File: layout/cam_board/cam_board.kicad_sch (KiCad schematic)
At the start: 76 parts, among them J2 USB Connector, J3 BATT_CONNECTOR, J4 LCD conn, J5 Stick conn, J6 Conn_01x05_Pin, SW1 BOOT0, SW2 NRST, SW3 USER, SW4 ON/OFF, U1 STM32F401CCUx, U2 USBLC6-2SC6, U3 M24C16-RMN6TP, U4 AP2112K-3.3, U5 MCP73871-1AA, Y1 ECS-80-18-23B-JTN-TR, Y2 SC32S-7PF20PPM

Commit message: Update board and layout
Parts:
- removed J6: Conn_01x05_Pin, Connector_PinHeader_1.27mm:PinHeader_1x05_P1.27mm_Vertical, symbol Connector:Conn_01x05_Pin
- added J1: Conn_01x06_Pin, Connector_PinHeader_1.27mm:PinHeader_1x06_P1.27mm_Vertical, symbol Connector:Conn_01x06_Pin
- added JP5, JP6: SolderJumper_2_Open, Jumper:SolderJumper-2_P1.3mm_Open_RoundedPad1.0x1.5mm, symbol Jumper:SolderJumper_2_Open
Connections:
- net +3V3: now also JP5.1 (A), JP6.2 (B); no longer C17.1, U4.5 (VOUT)
- net GND: now also J1.2 (Pin_2)
- net NRST: now also J1.6 (Pin_6)
- net SWCLK: now also J1.3 (Pin_3)
- net SWDIO: now also J1.4 (Pin_4)
- net SWO: now also J1.5 (Pin_5)
- new net: C17.1, JP6.1 (A), U4.5 (VOUT)
- new net: J1.1 (Pin_1), JP5.2 (B)

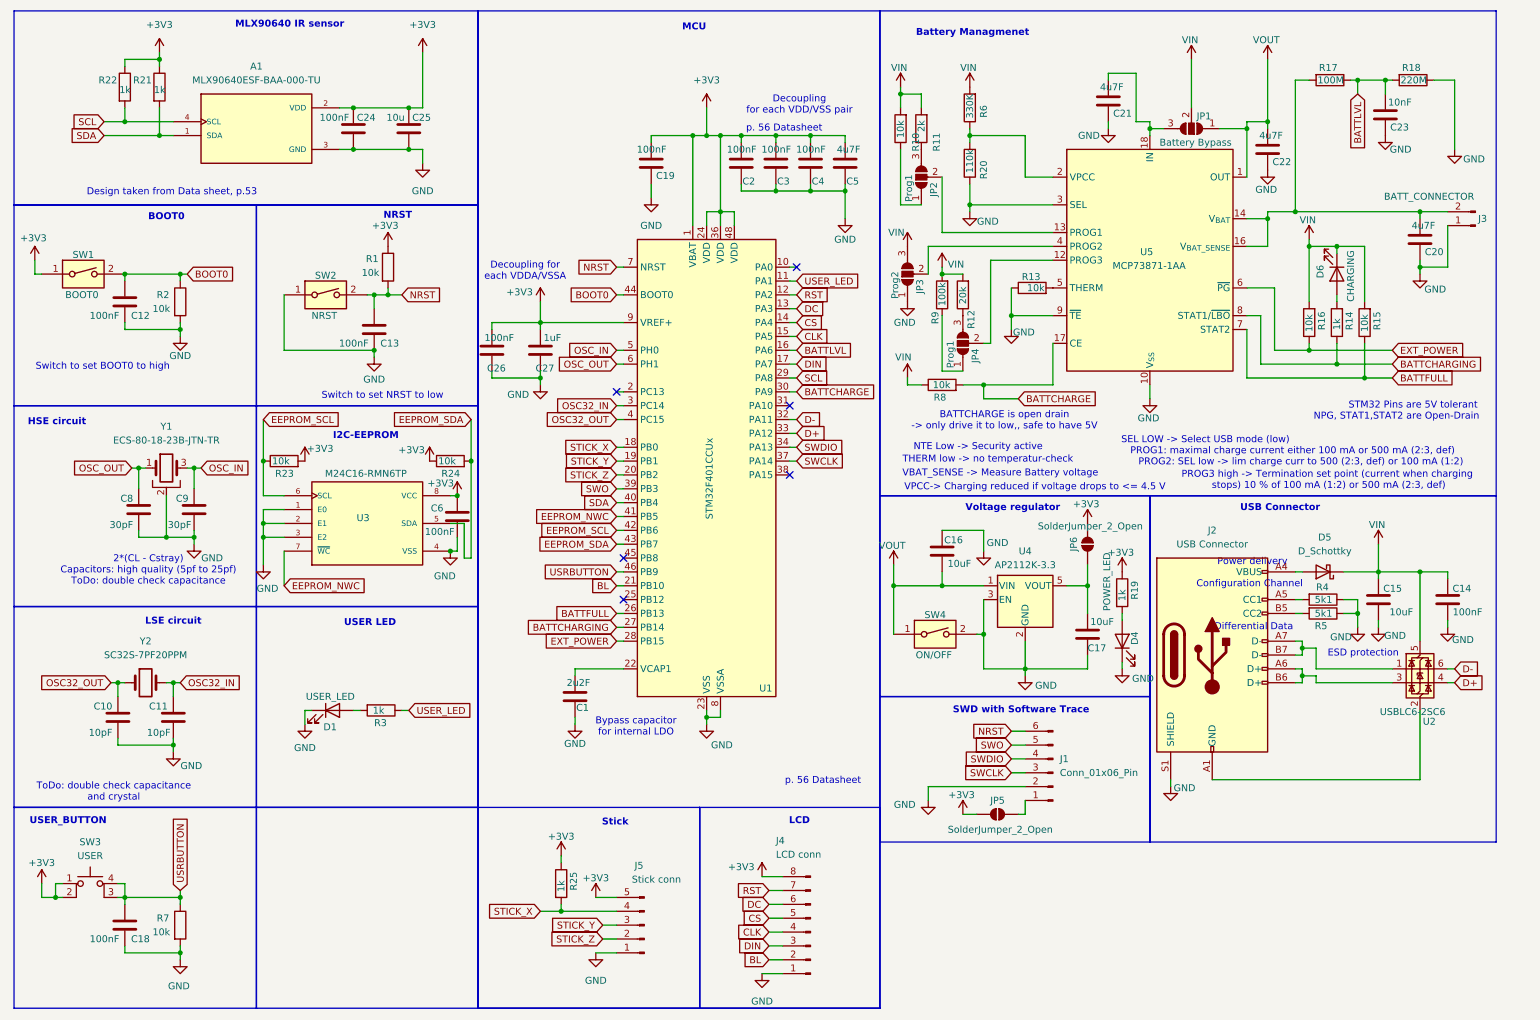
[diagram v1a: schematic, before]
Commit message: add to main loop, update layout and schematic
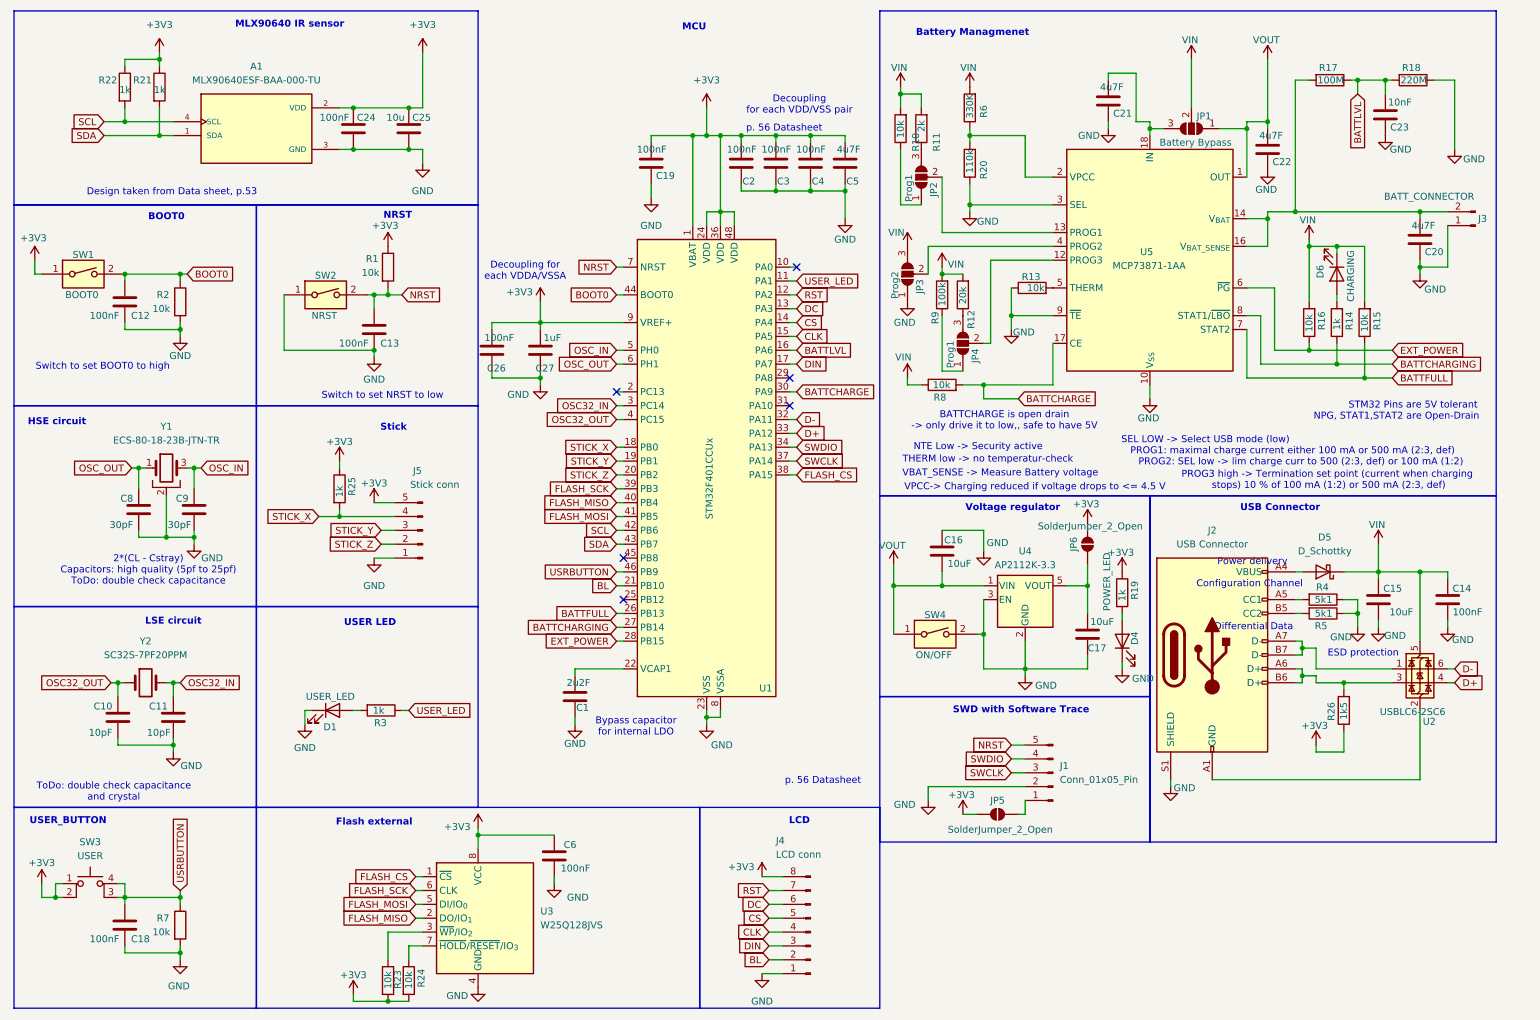
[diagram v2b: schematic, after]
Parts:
- removed J1: Conn_01x06_Pin, Connector_PinHeader_1.27mm:PinHeader_1x06_P1.27mm_Vertical, symbol Connector:Conn_01x06_Pin
- removed U3: M24C16-RMN6TP, A_Custom:SOIC127P600X175-8N, symbol Custom:M24C16-RMN6TP
- added J1: Conn_01x05_Pin, Connector_PinHeader_1.27mm:PinHeader_1x05_P1.27mm_Vertical, symbol Connector:Conn_01x05_Pin
- added R26: 1k5, Resistor_SMD:R_0603_1608Metric_Pad0.98x0.95mm_HandSolder, symbol Device:R
- added U3: W25Q128JVS, Package_SO:SOIC-8_5.3x5.3mm_P1.27mm, symbol Memory_Flash:W25Q128JVS
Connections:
- net +3V3: now also R24.2, R26.1, U3.8 (VCC); no longer R24.1
- net GND: now also J1.2 (Pin_2), U3.4 (GND)
- net NRST: now also J1.5 (Pin_5)
- net SCL: now also U1.42 (PB6); no longer U1.29 (PA8)
- net SDA: now also U1.43 (PB7); no longer U1.40 (PB4)
- net SWCLK: now also J1.3 (Pin_3)
- net SWDIO: now also J1.4 (Pin_4)
- net FLASH_CS: now reaches U1.38 (PA15)
- net FLASH_CS: now also U3.1 (~{CS})
- net at JP5.2 (B): now also J1.1 (Pin_1)
- net at J2.A6 (D+), J2.B6 (D+), U2.3 (I/O2): now also R26.2
- net EEPROM_NWC renamed FLASH_MOSI
- net FLASH_MOSI: now also U3.5 (DI/IO_{0})
- net EEPROM_SCL: no longer names the net of R23.1
- net EEPROM_SCL: now also U3.3 (~{WP}/IO_{2}); no longer U1.42 (PB6)
- removed net EEPROM_SDA: R24.2, U1.43 (PB7)
- net SWO renamed FLASH_SCK
- net FLASH_SCK: now also U3.6 (CLK)
- new net: R24.1, U3.7 (~{HOLD}/~{RESET}/IO_{3})
- new net FLASH_MISO: U1.40 (PB4), U3.2 (DO/IO_{1})
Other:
- note added: "Flash external"
- note removed: "I2C-EEPROM"
- moved on the sheet: J5, R25

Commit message: Update layout
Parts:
- added R27: 100k, Resistor_SMD:R_0603_1608Metric_Pad0.98x0.95mm_HandSolder, symbol Device:R
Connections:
- net GND: now also R27.1; no longer SW4.2, U4.3 (EN)
- new net: R27.2, SW4.2, U4.3 (EN)
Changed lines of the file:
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@@
 	)
 	(junction
+		(at 190.5 127)
+		(diameter 0)
+		(color 0 0 0 0)
+	)
+	(junction
 		(at 81.28 194.31)
 		(diameter 0)
@@
 	)
 	(junction
-		(at 190.5 127)
-		(diameter 0)
-		(color 0 0 0 0)
-	)
-	(junction
 		(at 238.76 34.29)
 		(diameter 0)
@@
 	)
 	(junction
-		(at 198.12 133.35)
+		(at 152.4 45.72)
 		(diameter 0)
 		(color 0 0 0 0)
 	)
 	(junction
-		(at 152.4 45.72)
+		(at 198.12 134.62)
 		(diameter 0)
 		(color 0 0 0 0)
@@
 	(wire
 		(pts
-			(xy 209.55 130.81) (xy 209.55 133.35)
+			(xy 209.55 130.81) (xy 209.55 134.62)
 		)
 		(stroke
@@
 	(wire
 		(pts
+			(xy 190.5 134.62) (xy 198.12 134.62)
+		)
+		(stroke
+			(width 0)
+			(type default)
+		)
+	)
+	(wire
+		(pts
 			(xy 139.7 142.24) (xy 139.7 143.51)
 		)
@@
 	(wire
 		(pts
-			(xy 209.55 133.35) (xy 198.12 133.35)
+			(xy 209.55 134.62) (xy 198.12 134.62)
 		)
 		(stroke
@@
 	(wire
 		(pts
-			(xy 198.12 134.62) (xy 198.12 133.35)
+			(xy 198.12 128.27) (xy 198.12 134.62)
 		)
 		(stroke
@@
 	(wire
 		(pts
-			(xy 190.5 127) (xy 190.5 133.35)
-		)
-		(stroke
-			(width 0)
-			(type default)
-		)
-	)
-	(wire
-		(pts
 			(xy 262.89 110.49) (xy 262.89 115.57)
 		)
@@
 	(wire
 		(pts
-			(xy 198.12 128.27) (xy 198.12 133.35)
-		)
-		(stroke
-			(width 0)
-			(type default)
-		)
-	)
-	(wire
-		(pts
 			(xy 179.07 30.48) (xy 179.07 27.94)
 		)
@@
 	(wire
 		(pts
-			(xy 190.5 133.35) (xy 198.12 133.35)
-		)
-		(stroke
-			(width 0)
-			(type default)
-		)
-	)
-	(wire
-		(pts
 			(xy 109.22 80.01) (xy 100.33 80.01)
 		)
@@
 					(unit 1)
 				)
+			)
+		)
+	)
+	(symbol
+		(lib_id "Device:R")
+		(at 190.5 130.81 180)
+		(unit 1)
+		(exclude_from_sim no)
+		(in_bom yes)
+		(on_board yes)
+		(dnp no)
+		(property "Reference" "R27"
+			(at 187.96 130.556 90)
+			(effects
+				(font
+					(size 1.27 1.27)
+				)
+				(justify left)
+			)
+		)
+		(property "Value" "100k"
+			(at 190.5 128.524 90)
+			(effects
+				(font
+					(size 1.27 1.27)
+				)
+				(justify left)
+			)
+		)
+		(property "Footprint" "Resistor_SMD:R_0603_1608Metric_Pad0.98x0.95mm_HandSolder"
+			(at 192.278 130.81 90)
+			(effects
+				(font
+					(size 1.27 1.27)
+				)
+				(hide yes)
+			)
+		)
+		(property "Datasheet" "~"
+			(at 190.5 130.81 0)
+			(effects
+				(font
+					(size 1.27 1.27)
+				)
+				(hide yes)
+			)
+		)
+		(property "Description" "Resistor"
+			(at 190.5 130.81 0)
+			(effects
+				(font
+					(size 1.27 1.27)
+				)
+				(hide yes)
+			)
+		)
+		(pin "2"
+		)
+		(pin "1"
+		)
+		(instances
+			(project "cam_board"
+				(path "/eee23683-93c4-45fa-9c00-e358d0d25f58"
+					(reference "R27")
+					(unit 1)
+				)

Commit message: Update
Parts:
- removed SW2: NRST, Button_Switch_SMD:SW_DIP_SPSTx01_Slide_6.7x4.1mm_W8.61mm_P2.54mm_LowProfile, symbol Switch:SW_DIP_x01
- added SW3: NRST, A_Custom:SW_1825910-6-4, symbol Switch:SW_MEC_5E
- renumbered C10 to C1, C26 to C10, C27 to C11, C6 to C12, C1 to C13, C19 to C14, C2 to C15, C3 to C16, C4 to C17, C5 to C18, C16 to C19, C12 to C2, C17 to C20, C15 to C23, C23 to C24, C20 to C25, C14 to C26, C18 to C3, C8 to C4, C11 to C5, C9 to C6, C24 to C7, C13 to C8, C25 to C9, D4 to D2, D5 to D3, D6 to D4, J5 to J1, J4 to J2, J1 to J3, J2 to J4, J3 to J5, JP3 to JP1, JP4 to JP3, JP5 to JP4, JP6 to JP5, JP1 to JP6, R22 to R1, R9 to R12, R8 to R13, R12 to R14, R6 to R15, R20 to R16, R27 to R17, R13 to R18, R21 to R2, R16 to R20, R4 to R21, R5 to R22, R17 to R23, R14 to R24, R26 to R25, R15 to R26, R18 to R27, R2 to R3, R7 to R4, R25 to R5, R3 to R6, R1 to R7, R23 to R8, R24 to R9, SW3 to SW2, U3 to U1, U1 to U2, U4 to U3, U5 to U4, U2 to U5, Y2 to Y1, Y1 to Y2
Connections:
- net GND: now also SW3.1, SW3.2
- net NRST: now also SW3.3 (K), SW3.4 (A)

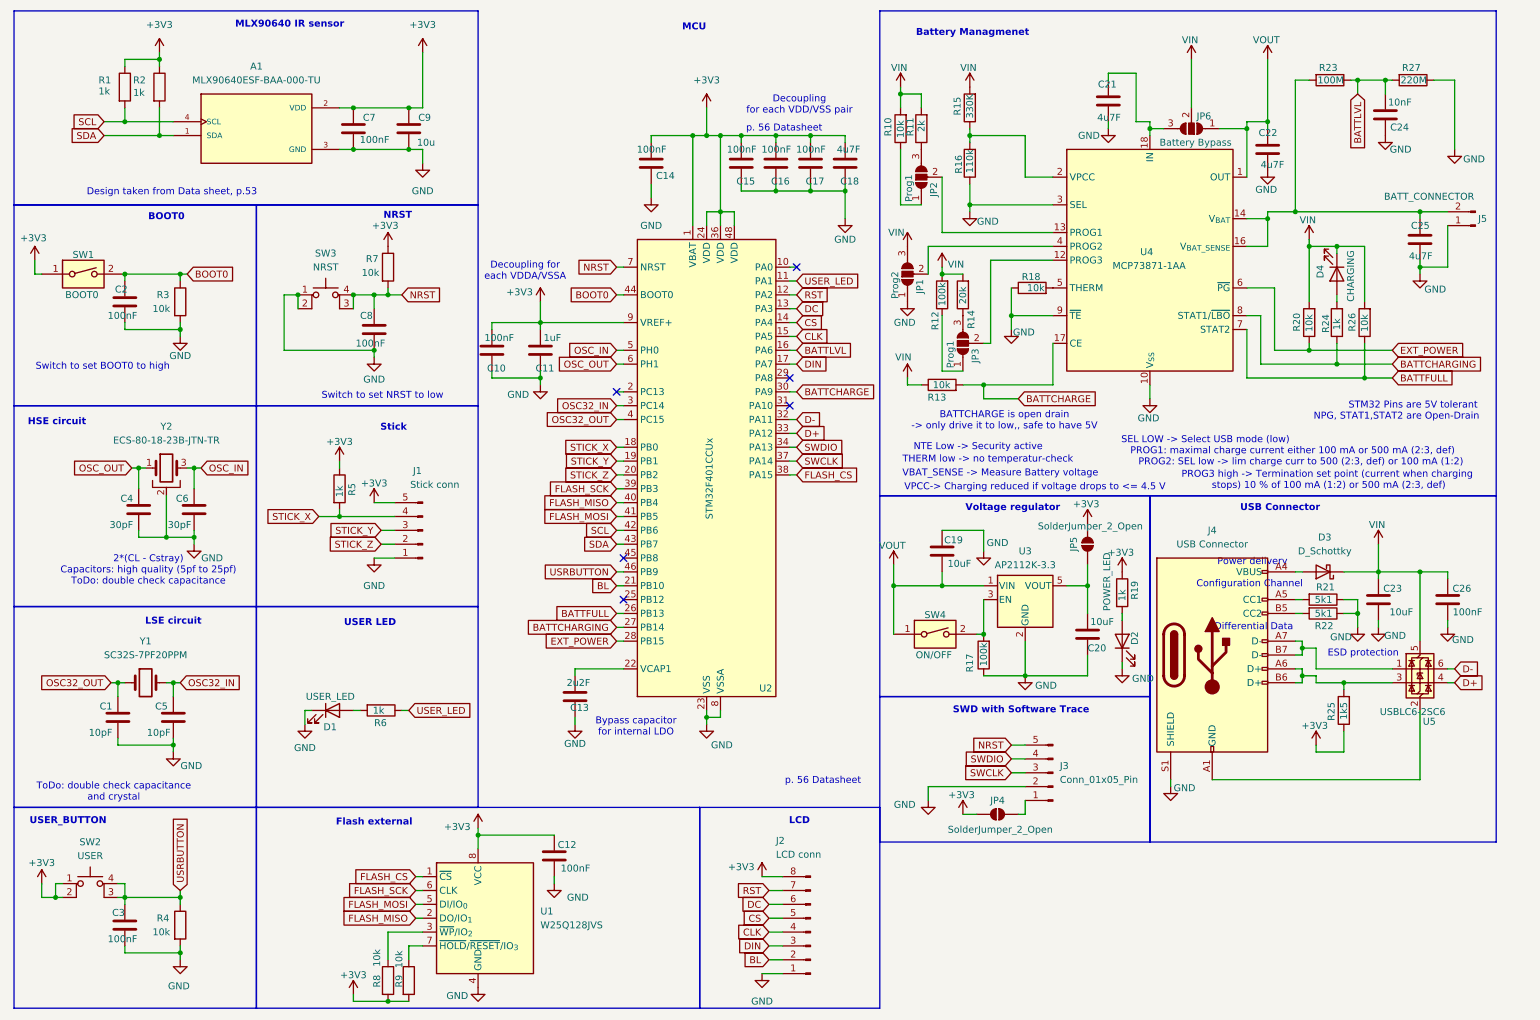
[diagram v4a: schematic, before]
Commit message: Changed foot print to 0603 for allk capacitors Changed footprints for connectors to 2.54 mm Fixed footprint of 32 MHz crystal / Y1 Change slider footprint from SMD to THT Remove USB pull up 1k5 Introduce Keep-Out zone
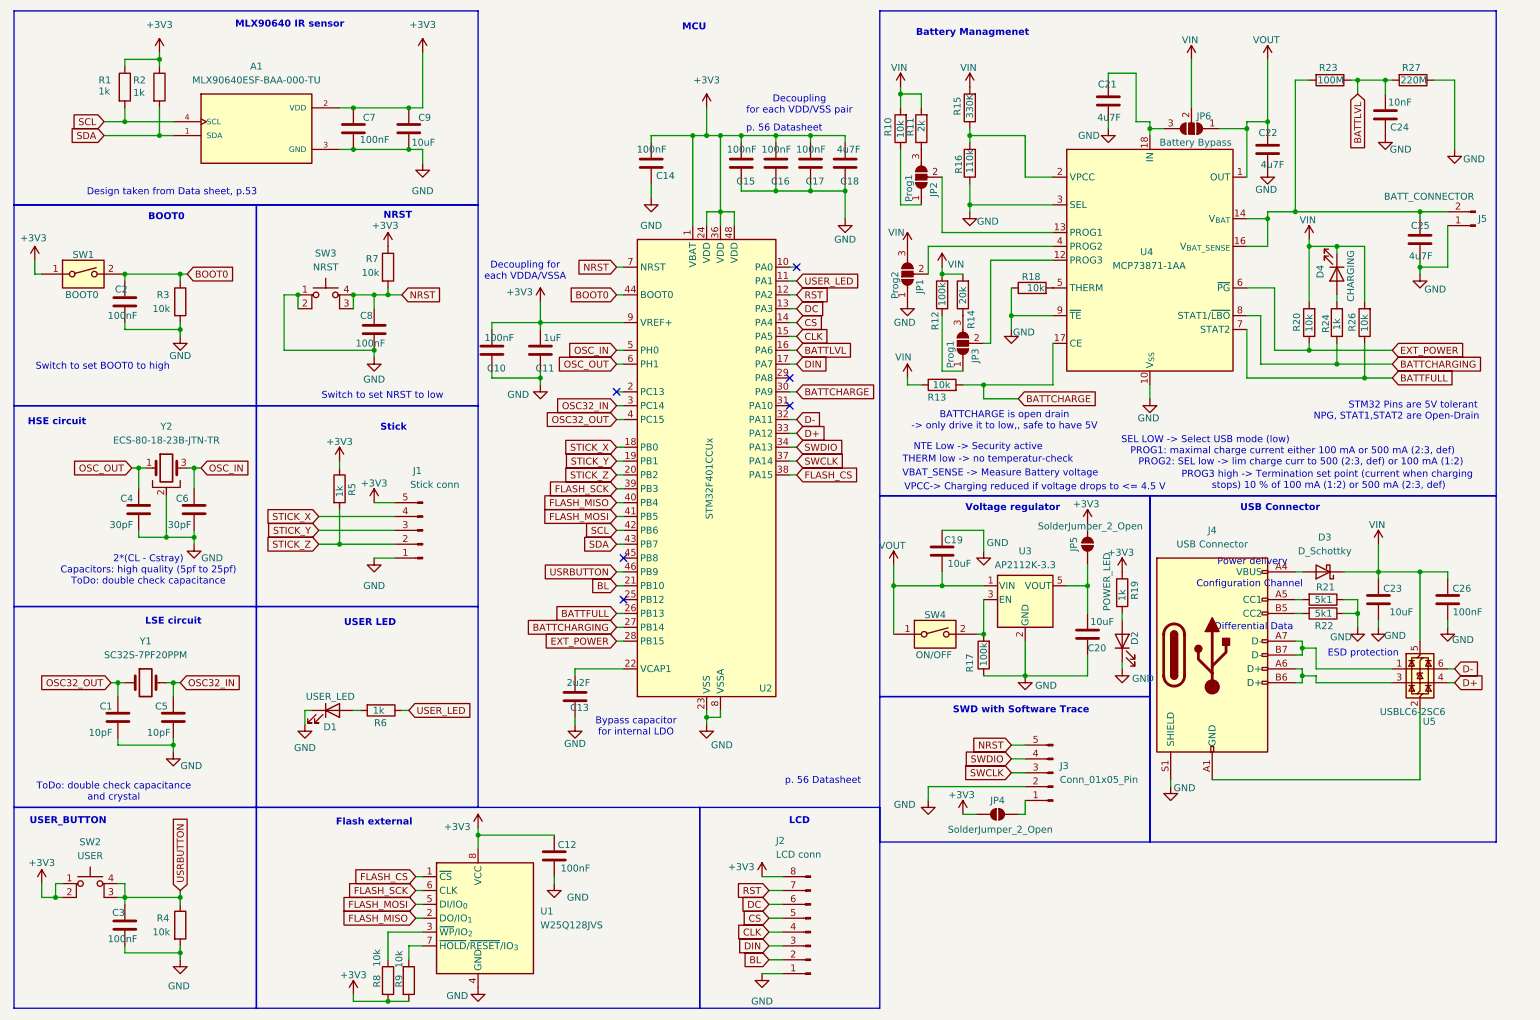
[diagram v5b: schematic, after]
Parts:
- removed R25: 1k5, Resistor_SMD:R_0603_1608Metric_Pad0.98x0.95mm_HandSolder, symbol Device:R
- C1, C10, C11, C13, C14, C15, C16, C17, C18, C24, C4, C5, C6: footprint Capacitor_SMD:C_0402_1005Metric_Pad0.74x0.62mm_HandSolder -> Capacitor_SMD:C_0603_1608Metric_Pad1.08x0.95mm_HandSolder
- C9: value 10u -> 10uF
- J1, J3: footprint Connector_PinHeader_1.27mm:PinHeader_1x05_P1.27mm_Vertical -> Connector_PinHeader_2.54mm:PinHeader_1x05_P2.54mm_Vertical
- J2: footprint Connector_PinHeader_1.27mm:PinHeader_1x08_P1.27mm_Vertical -> Connector_PinHeader_2.54mm:PinHeader_1x08_P2.54mm_Vertical
- SW1: footprint Button_Switch_SMD:SW_DIP_SPSTx01_Slide_6.7x4.1mm_W8.61mm_P2.54mm_LowProfile -> Button_Switch_THT:SW_DIP_SPSTx01_Slide_9.78x4.72mm_W7.62mm_P2.54mm
- Y1: footprint A_Custom:XTAL_CM8V-T1A-32.768KHZ-6PF-20PPM-TA-QC -> A_Custom:XTAL_CTS3-32.768-12.5-20-CT
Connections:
- net STICK_X: no longer R5.2
- net STICK_Z: now also R5.2

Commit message: Update
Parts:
- removed Y2: ECS-80-18-23B-JTN-TR, A_Custom:XTAL_ECS-80-18-23B-JTN-TR, symbol Device:Crystal_GND2
- added Y2: ECS-80-18-23B-JTN-TR, A_Custom:XTAL_ECS-80-18-23B-JTN-TR, symbol Custom:ECS-80-18-23B-JTN-TR
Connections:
- net GND: now also Y2.2 (GND), Y2.4 (GND)
- net OSC_IN: now also C4.2, Y2.1 (IN/OUT); no longer C6.2
- net OSC_OUT: now also C6.2, Y2.3 (OUT/IN); no longer C4.2
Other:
- note added: "2*(CL - Cstray) Capacitors: high quality"
- note removed: "2*(CL - Cstray) Capacitors: high quality (5pf to 25pf) ToDo: double check capacitance"
- moved on the sheet: C4, C6

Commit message: Update / version B
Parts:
- added JP7: Battery Bypass 2, Jumper:SolderJumper-2_P1.3mm_Open_RoundedPad1.0x1.5mm, symbol Jumper:SolderJumper_2_Open
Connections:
- net VOUT: now also JP7.2 (B); no longer U4.1 (OUT), U4.20 (OUT)
- new net: JP7.1 (A), U4.1 (OUT), U4.20 (OUT)
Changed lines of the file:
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@@
 	)
 	(junction
-		(at 238.76 34.29)
+		(at 270.51 59.69)
 		(diameter 0)
 		(color 0 0 0 0)
 	)
 	(junction
-		(at 270.51 59.69)
+		(at 152.4 45.72)
 		(diameter 0)
 		(color 0 0 0 0)
 	)
 	(junction
-		(at 152.4 45.72)
+		(at 198.12 134.62)
 		(diameter 0)
 		(color 0 0 0 0)
 	)
 	(junction
-		(at 198.12 134.62)
+		(at 238.76 34.29)
 		(diameter 0)
 		(color 0 0 0 0)
@@
 	(wire
 		(pts
+			(xy 238.76 41.91) (xy 238.76 43.18)
+		)
+		(stroke
+			(width 0)
+			(type default)
+		)
+	)
+	(wire
+		(pts
 			(xy 195.58 71.12) (xy 195.58 68.58)
 		)
@@
 	(wire
 		(pts
-			(xy 238.76 34.29) (xy 238.76 43.18)
-		)
-		(stroke
-			(width 0)
-			(type default)
-		)
-	)
-	(wire
-		(pts
 			(xy 250.19 73.66) (xy 250.19 74.93)
 		)
@@
 					(unit 1)
 				)
+			)
+		)
+	)
+	(symbol
+		(lib_id "Jumper:SolderJumper_2_Open")
+		(at 238.76 38.1 90)
+		(unit 1)
+		(exclude_from_sim no)
+		(in_bom no)
+		(on_board yes)
+		(dnp no)
+		(property "Reference" "JP7"
+			(at 238.506 41.148 90)
+			(effects
+				(font
+					(size 1.27 1.27)
+				)
+			)
+		)
+		(property "Value" "Battery Bypass 2"
+			(at 241.046 30.734 90)
+			(effects
+				(font
+					(size 1.27 1.27)
+				)
+			)
+		)
+		(property "Footprint" "Jumper:SolderJumper-2_P1.3mm_Open_RoundedPad1.0x1.5mm"
+			(at 238.76 38.1 0)
+			(effects
+				(font
+					(size 1.27 1.27)
+				)
+				(hide yes)
+			)
+		)
+		(property "Datasheet" "~"
+			(at 238.76 38.1 0)
+			(effects
+				(font
+					(size 1.27 1.27)
+				)
+				(hide yes)
+			)
+		)
+		(property "Description" "Solder Jumper, 2-pole, open"
+			(at 238.76 38.1 0)
+			(effects
+				(font
+					(size 1.27 1.27)
+				)
+				(hide yes)
+			)
+		)
+		(pin "1"
+		)
+		(pin "2"
+		)
+		(instances
+			(project "cam_board"
+				(path "/eee23683-93c4-45fa-9c00-e358d0d25f58"
+					(reference "JP7")
+					(unit 1)
+				)
